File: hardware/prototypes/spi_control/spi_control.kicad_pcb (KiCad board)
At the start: 4 copper layers, 66.9 x 43.2 mm, 85 parts, among them J1 USB_B_Micro, J39 Versa_1, J40 Versa_2, U1 ST1L08SPU33R, U2 MCP2210-I_MQ, U3 ADAR7251, U4 BGT24_Module, Y1 12MHZ, Y2 40MHz

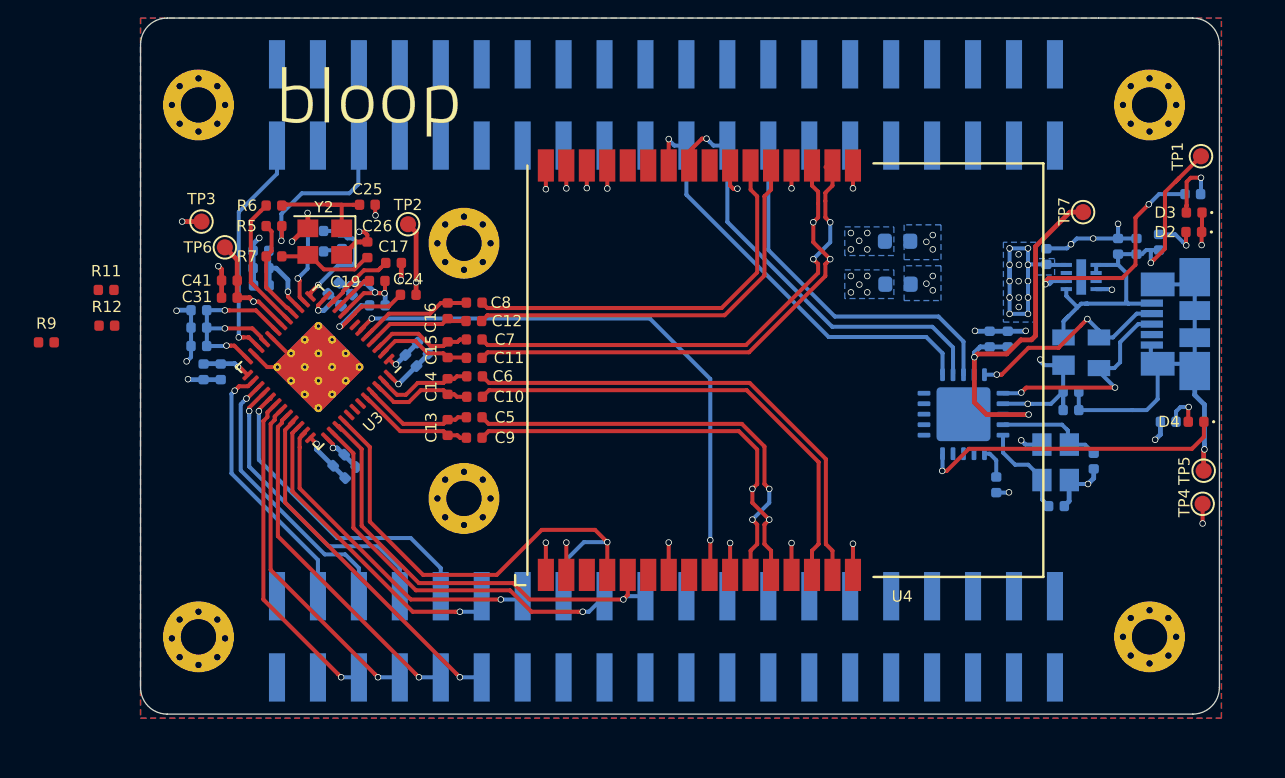
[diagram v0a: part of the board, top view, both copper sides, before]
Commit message: Finished, DRC approved,  All nets routed.
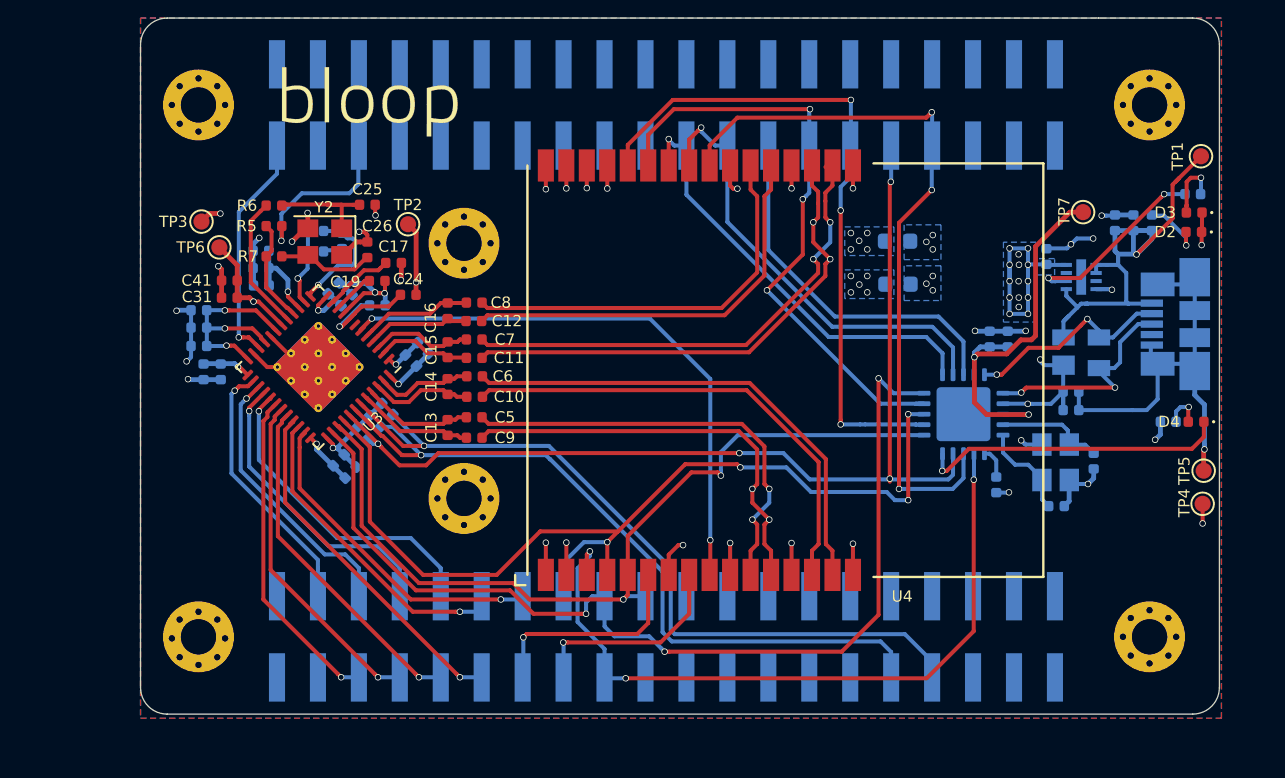
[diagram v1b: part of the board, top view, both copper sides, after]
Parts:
- R11, R12, R9: moved to B.Cu
- moved R9 20.4 mm to (71.2, 80.4), turned to 315 degrees
- moved R11 18.6 mm to (71.9, 79.6), turned to 315 degrees
- moved R12 18.1 mm to (72.7, 78.9), turned to 315 degrees
- moved C2 1.47 mm to (117.9, 67.3)
- moved C3 1.47 mm to (119.0, 67.3)
- moved R2 1.29 mm to (120.1, 67.3)
- moved TP6 0.34 mm to (62.3, 68.8)
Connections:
- J39 pad 13: /PLL_DIV_MCU -> /PLL_LE
- J39 pad 15: /PLL_LE -> /PLL_DIV_MCU
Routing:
- net /~ADC_CS: track 0.00 -> 62.8 mm, vias 0 -> 4
- net /~RESET\PWDN: track 0.00 -> 48.1 mm, vias 0 -> 1
- net /~FAULT: track 0.00 -> 46.5 mm, vias 0 -> 1
- net /~BGT_CS: track 0.00 -> 45.9 mm, vias 0 -> 3
- net /PLL_CS: track 0.00 -> 45.5 mm, vias 0 -> 3
- net /PLL_TRIG1: track 0.00 -> 41.8 mm, vias 0 -> 3
- net /MISO: track 24.6 -> 63.5 mm, vias 1 -> 3
- net /PLL_TRIG2: track 0.00 -> 38.1 mm, vias 0 -> 3
- net /SCK: track 31.9 -> 60.1 mm, vias 1 -> 4
- net /MOSI: track 28.0 -> 52.5 mm, vias 1 -> 2
- net /PLL_LE: track 0.00 -> 13.6 mm, vias 0 -> 1
- net /PLL_DIV_MCU: track 0.00 -> 13.1 mm, vias 0 -> 1
- net /5V_USB: track 26.4 -> 31.7 mm
- net +3V3: track 46.8 -> 51.0 mm
- net Net-(R3-Pad2): track 14.2 -> 11.8 mm
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
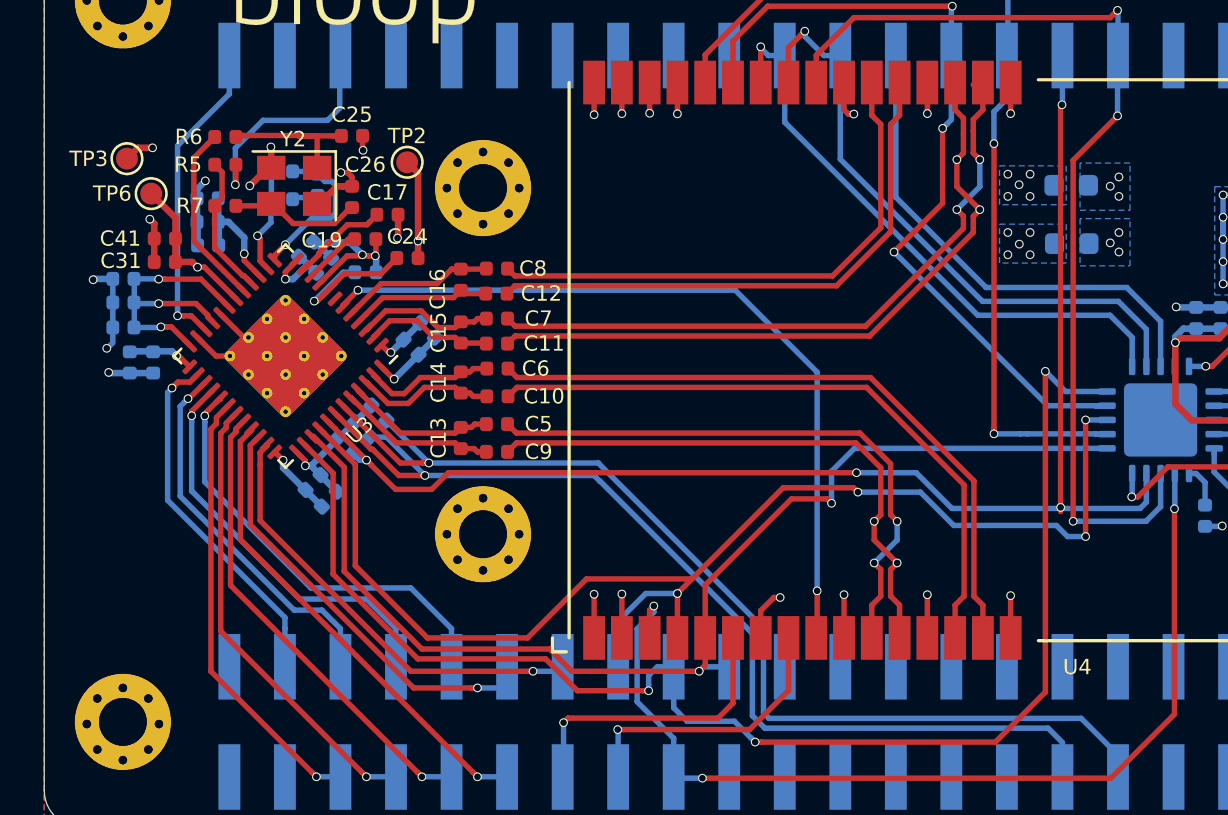
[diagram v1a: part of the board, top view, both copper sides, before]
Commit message: Fixed gnd patch on ADAR ADC footprint
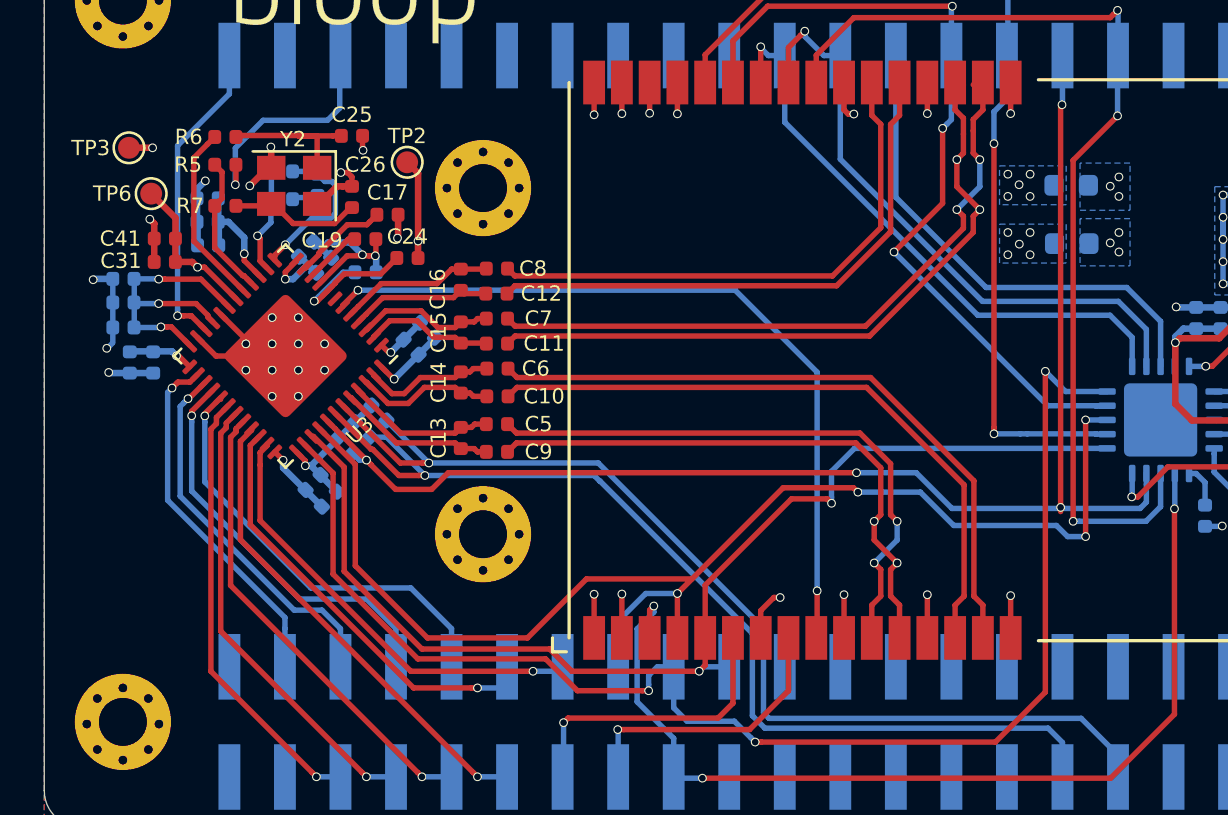
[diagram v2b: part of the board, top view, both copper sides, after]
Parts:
- U3: footprint Package_CSP:LFCSP-48-1EP_7x7mm_P0.5mm_EP4.1x4.1mm_ThermalVias -> Package_CSP:LFCSP-48-1EP_7x7mm_P0.5mm_EP4.1x4.1mm
- moved TP3 0.50 mm to (61.3, 66.7)
- renumbered U4 to <-
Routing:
- net GND: track 54.0 -> 53.3 mm, vias 24 -> 36

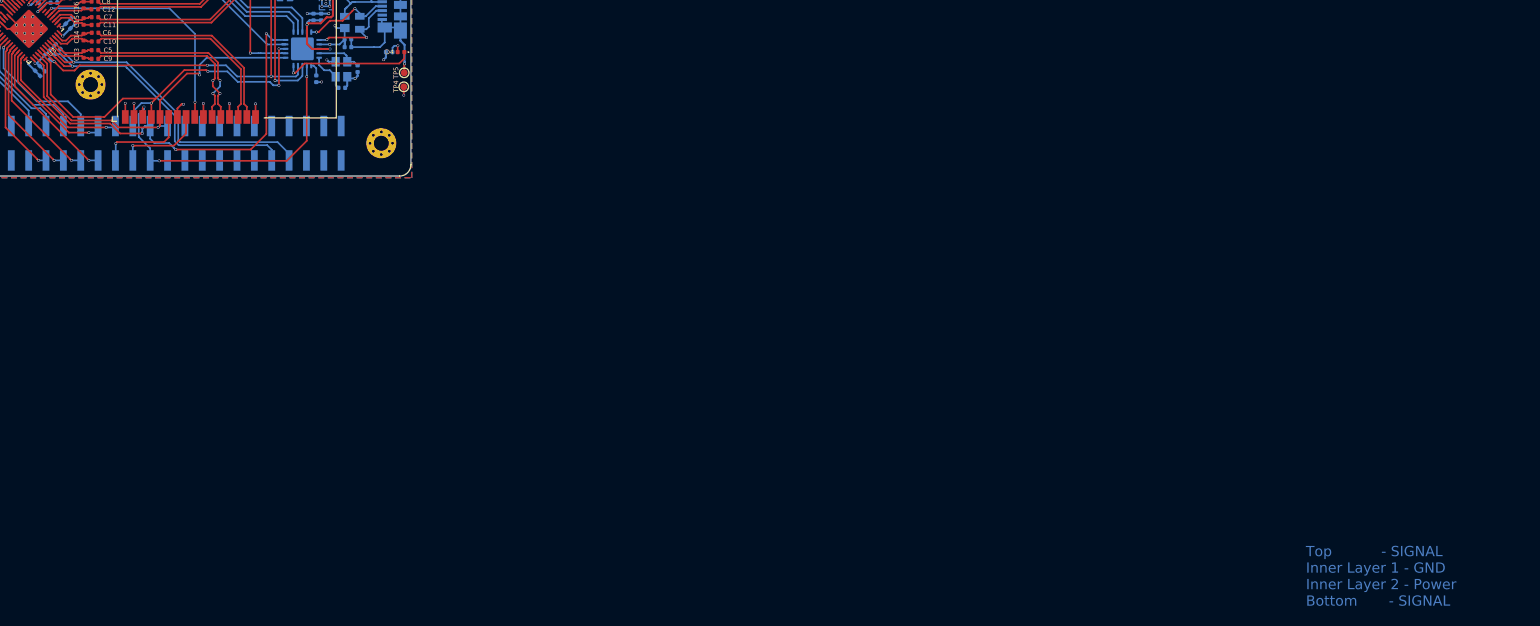
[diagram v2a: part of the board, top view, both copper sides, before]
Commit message: Added 3d model for ADAR7251 and moved footprint into bloop.pretty. Updated schematic, J39-13 swaped with J39-15. Corrected stackup text in layout to ECO1 layer from BCu.
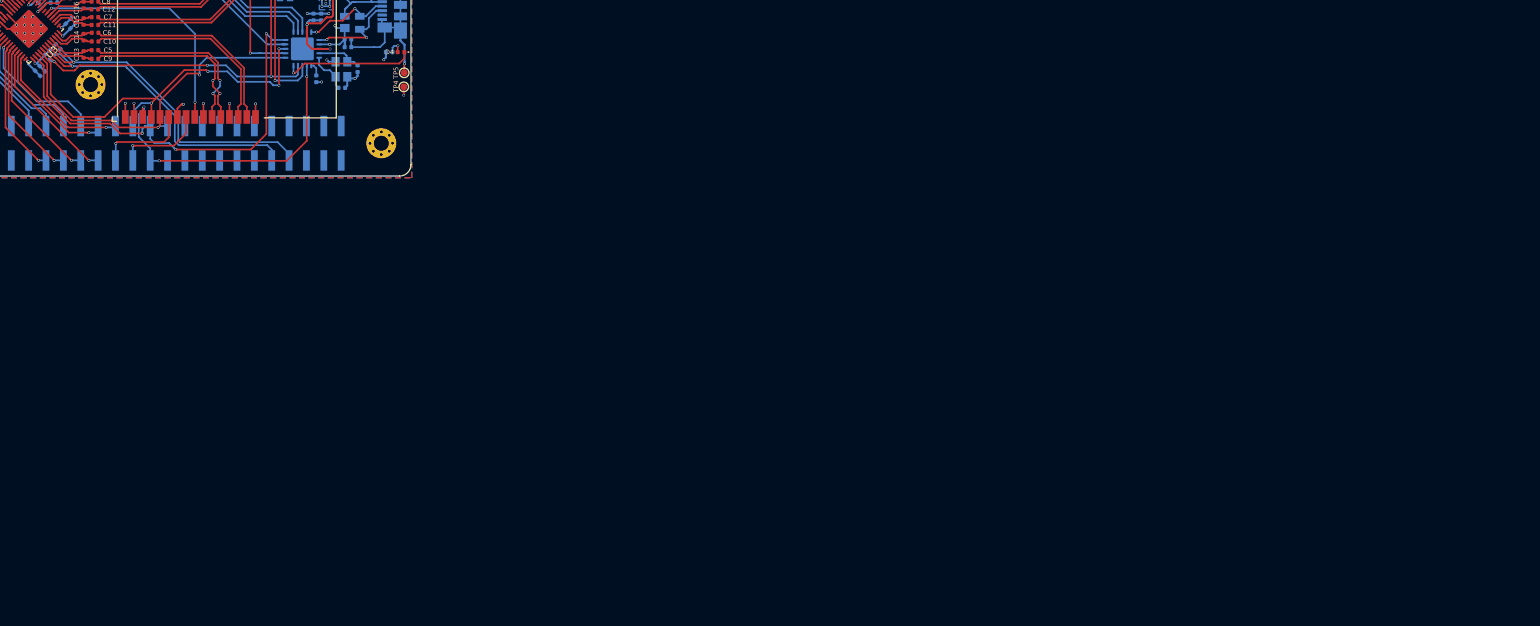
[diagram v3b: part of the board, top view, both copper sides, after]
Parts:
- U3: footprint Package_CSP:LFCSP-48-1EP_7x7mm_P0.5mm_EP4.1x4.1mm -> bloop:LFCSP-48-1EP_7x7mm_P0.5mm_EP4.1x4.1mm
- renumbered <- to U4

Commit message: Added wonderful Silkscreen to the bottom
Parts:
- added G***: LOGO, bloop:meseek, B.Cu at (92.2, 74.4)
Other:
- board text added: "Dime for Scale"

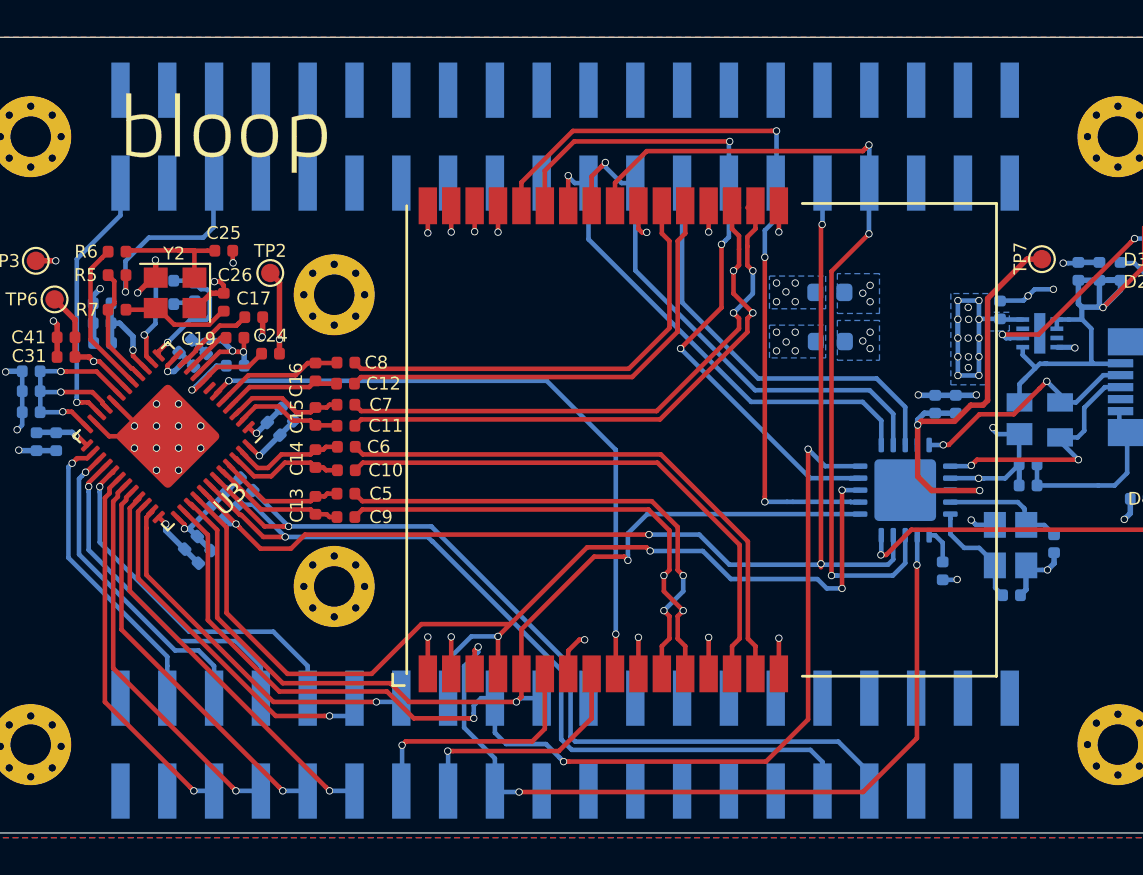
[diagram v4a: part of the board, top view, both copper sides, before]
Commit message: Found mistake in header breakout, grounds were not connected. Fixed, layout and schematic.
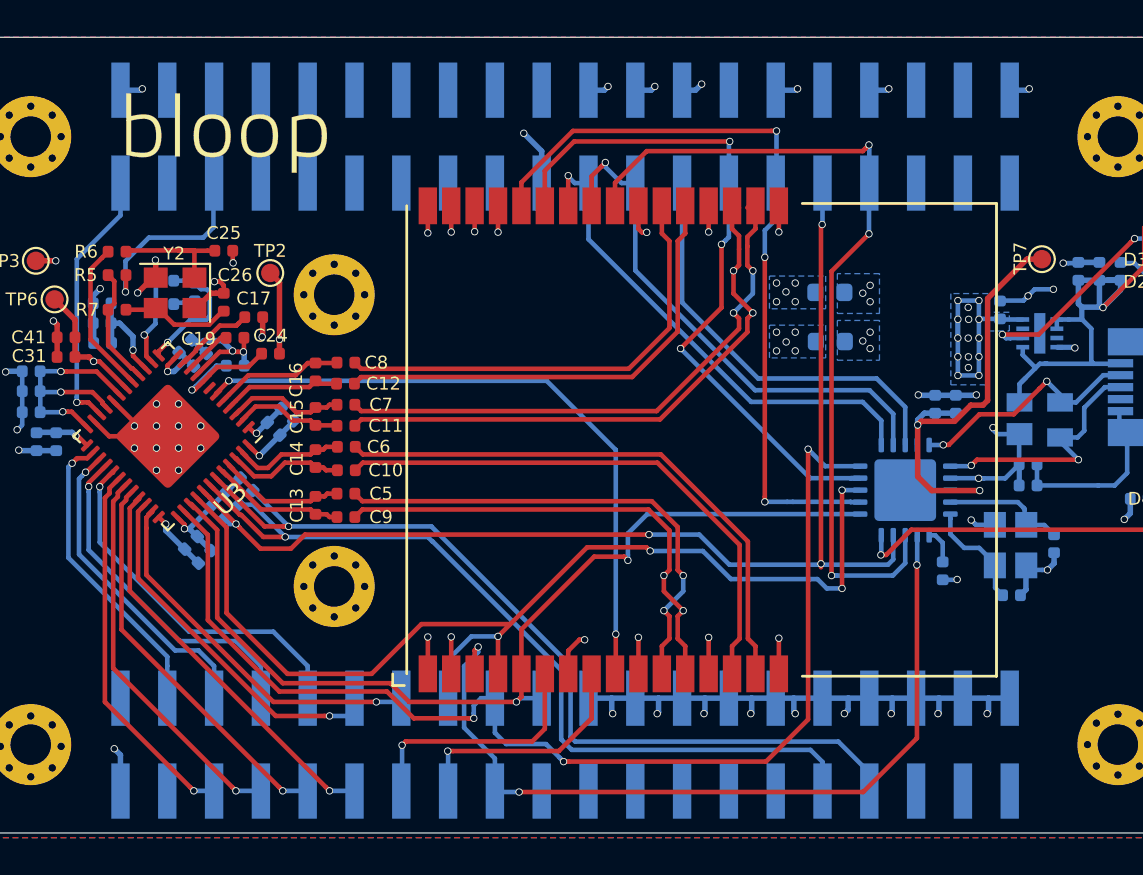
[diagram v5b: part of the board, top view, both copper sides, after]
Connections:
- J39 pad 1: Net-(J39-Pad1) -> GND
- J39 pad 22: Net-(J39-Pad22) -> GND
- J39 pad 24: Net-(J39-Pad24) -> GND
- J39 pad 26: Net-(J39-Pad26) -> GND
- J39 pad 28: Net-(J39-Pad28) -> GND
- J39 pad 30: Net-(J39-Pad30) -> GND
- J39 pad 32: Net-(J39-Pad32) -> GND
- J39 pad 34: Net-(J39-Pad34) -> GND
- J39 pad 36: Net-(J39-Pad36) -> GND
- J39 pad 38: Net-(J39-Pad38) -> GND
- J39 pad 40: Net-(J39-Pad40) -> GND
- J40 pad 19: Net-(J40-Pad19) -> GND
- J40 pad 2: Net-(J40-Pad2) -> GND
- J40 pad 22: Net-(J40-Pad22) -> GND
- J40 pad 24: Net-(J40-Pad24) -> GND
- J40 pad 26: Net-(J40-Pad26) -> GND
- J40 pad 30: Net-(J40-Pad30) -> GND
- J40 pad 34: Net-(J40-Pad34) -> GND
- J40 pad 40: Net-(J40-Pad40) -> GND
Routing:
- net GND: track 53.3 -> 97.6 mm, vias 36 -> 54

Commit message: Remove Dime scale. Fill on Top layer has no net.  GND Fill on Bottom layer has no net. GND Schematic: Clean up the ground connections on J40, J39, Y2, and Y1. Schematic: Remove ECP5 eval board schematic image. Need to generate BOM. Add NC to J39 and J40 where needed. Change directory “gerbers” to “spi_control_FAB”
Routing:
- added copper zone on F.Cu, net GND
- removed copper zone on B.Cu, net (none)
- removed copper zone on F.Cu, net (none)
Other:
- board text removed: "Dime for Scale"
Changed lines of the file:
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@@
   (general
     (thickness 1.6)
-    (drawings 16)
+    (drawings 14)
     (tracks 1122)
     (zones 0)
@@
     (last_trace_width 0.25)
     (trace_clearance 0.2)
-    (zone_clearance 0.2)
+    (zone_clearance 0.3)
     (zone_45_only no)
     (trace_min 0.2)
@@
     )
   )
-  (gr_text "Dime\n for Scale\n" (at 136.2202 83.7946) (layer Eco1.User)
-    (effects (font (size 1 1) (thickness 0.15)))
-  )
-  (gr_circle (center 136.5758 83.4898) (end 145.5758 83.4898) (layer Eco1.User) (width 0.15))
   (gr_line (start 255.27 163.83) (end 255.27 151.13) (layer Eco1.User) (width 0.15))
   (gr_line (start 283.21 163.83) (end 255.27 163.83) (layer Eco1.User) (width 0.15))
@@
     )
   )
-  (zone (net 0) (net_name "") (layer F.Cu) (hatch edge 0.508)
+  (zone (net 1) (net_name GND) (layer F.Cu) (hatch edge 0.508)
     (connect_pads yes (clearance 0.3))
     (min_thickness 0.254)
@@
     )
   )
-  (zone (net 0) (net_name "") (layer B.Cu) (hatch edge 0.508)
+  (zone (net 1) (net_name GND) (layer B.Cu) (hatch edge 0.508)
     (connect_pads yes (clearance 0.3))
     (min_thickness 0.254)
